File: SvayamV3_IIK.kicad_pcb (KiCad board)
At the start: 6 copper layers, 131.4 x 90 mm, 290 parts, among them J1 USB_C_Receptacle_USB2.0_16P, J10 Micro_SD_Card_Det1, J11 BUZZER, J12 ADC, J13 CAN, J14 SERIAL5, J15 SAFETY, J16 POWER2, J17 I2C, J18 CAN2, J19 Channel 1, J2 GPS, J20 Channel 5, J21 Channel 9, J22 Channel 13, J23 Channel 2, J24 Channel 6, J25 Channel 10, J26 Channel 14, J27 Channel 3, J28 Channel 7, J29 Channel 11, J3 SPI, J30 Channel 15, J31 Channel 4, J32 Channel 8, J33 Channel 12, J34 Channel 16, J4 TELEM1, J5 TELEM2, J6 SBUS, J7 Conn_01x05_Pin, J8 SERIAL4, J9 POWER1, Q1 AO3400A, SW1 SK-3296S-01-L3, SW2 TS-1010A-B, U1 STM32H743IIK6, U10 TPS2120YFPR, U11 TPS63070, U12 RT9080-33GJ5, U13 RT9080-33GJ5, U14 AP22804AW5, U15 USBLC6-2SC6, U16 TPS2553DBVT, U17 TPS2553DBVT, U18 TPS2553DBVT, U19 TPS2553DBVT, U2 FM25CL64B, U20 TPS2553DBVT, U21 TPS2553DBVT, U22 TPS2553DBVT, U23 TPS2553DBVT, U24 TPS2553DBVT, U3 TJA1051TK-3, U4 TJA1051TK-3, U5 BMP388, U6 DPS310XTSA1, U7 BMI088, U8 BMI270, U9 BMM150, Y1 X50328MSB2GI

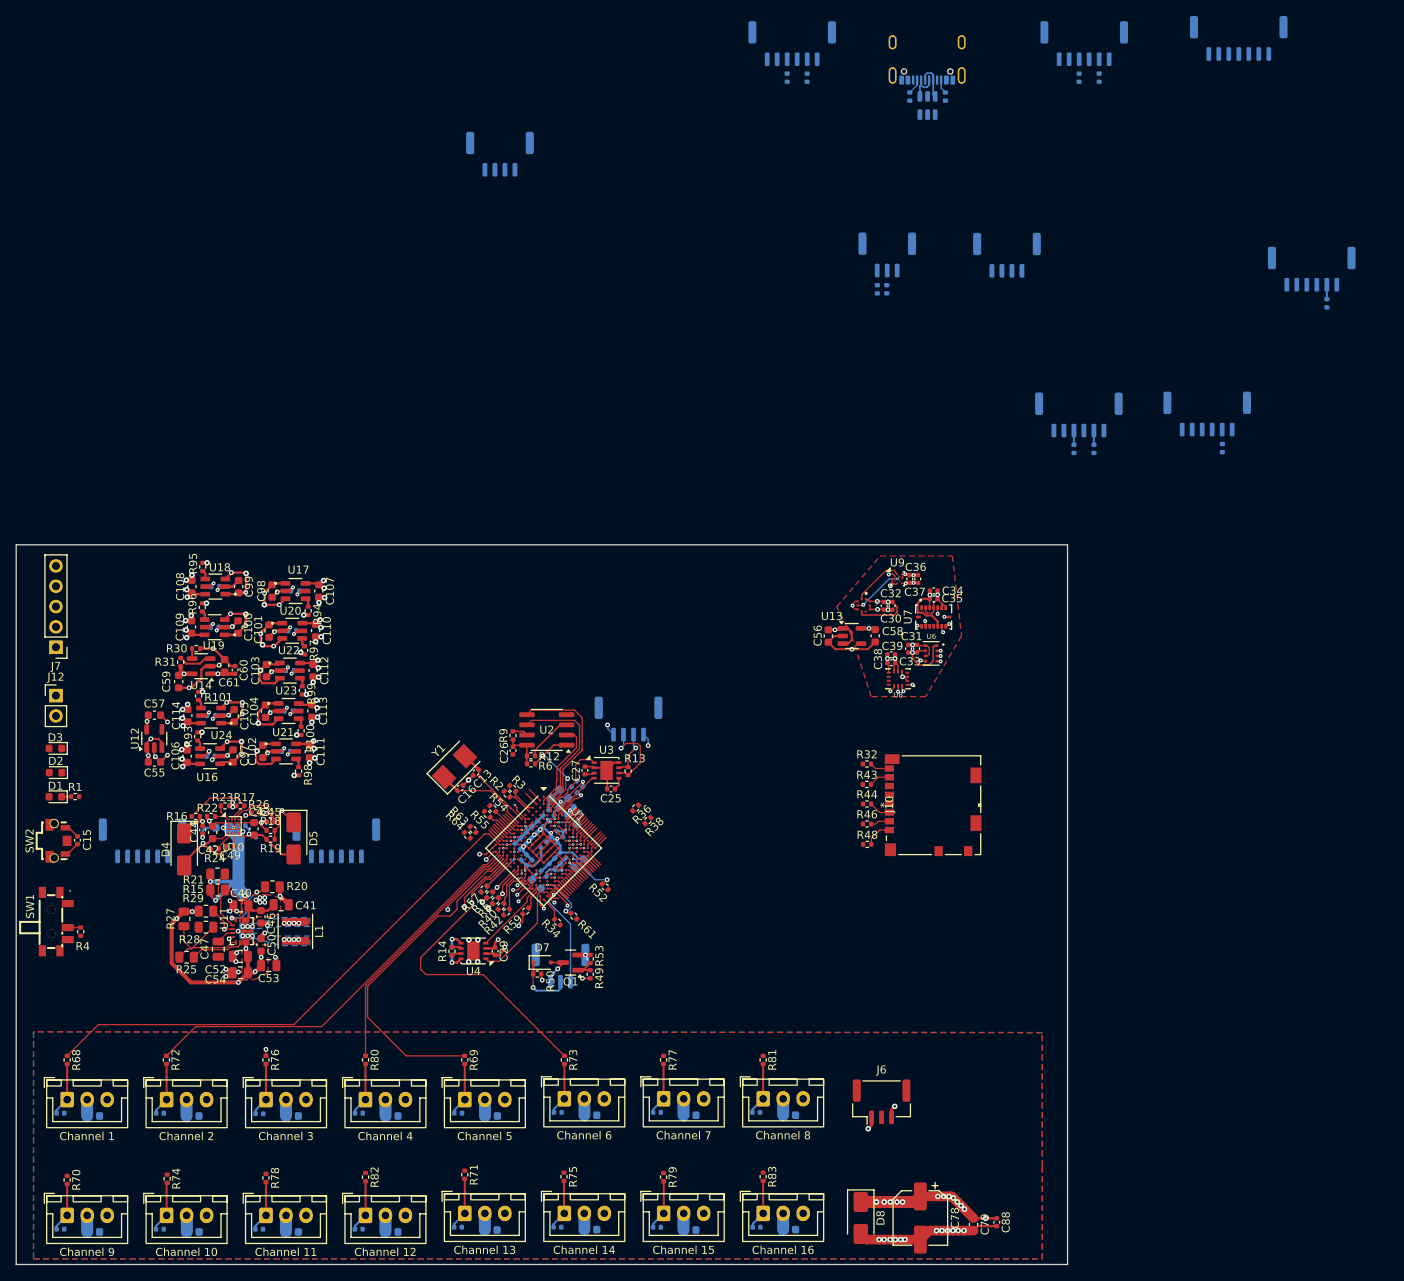
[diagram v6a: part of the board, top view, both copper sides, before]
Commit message: Repo: siap publikasi — README, docs/ (STATUS·DESIGN·STACKUP·schematic·BOM·report), fabrication gate, .gitignore/.gitattributes
- README.md: spesifikasi board, arsitektur, peta konektor, status jujur (not fab-ready)
- docs/: STATUS.md (DRC 765 item + 6 short terdaftar), DESIGN.md (keputusan + referensi),
  STACKUP.md (6-layer 1.5584mm terverifikasi), schematic.pdf, bom.csv, board-stats.txt,
  images/ (preview PCB F+B), reports/ (ERC + DRC mentah, bertanggal)
- fabrication/README.md: release gate + perintah ekspor gerber/drill/pos/step
- .gitignore: whitelist + blokir .history/ output/ *-backups/ *.kicad_prl *.lck
- untrack: .kicad_prl, 23 backup zip, Library/tps63070.pretty/catboy.kicad_mod (0 referensi)

Verifikasi: ERC 0E/17W, parity 0, 290 fp/262 net/1005 node, DRC 765 (6 short, 7 unconnected) — kicad-cli 10.0.6
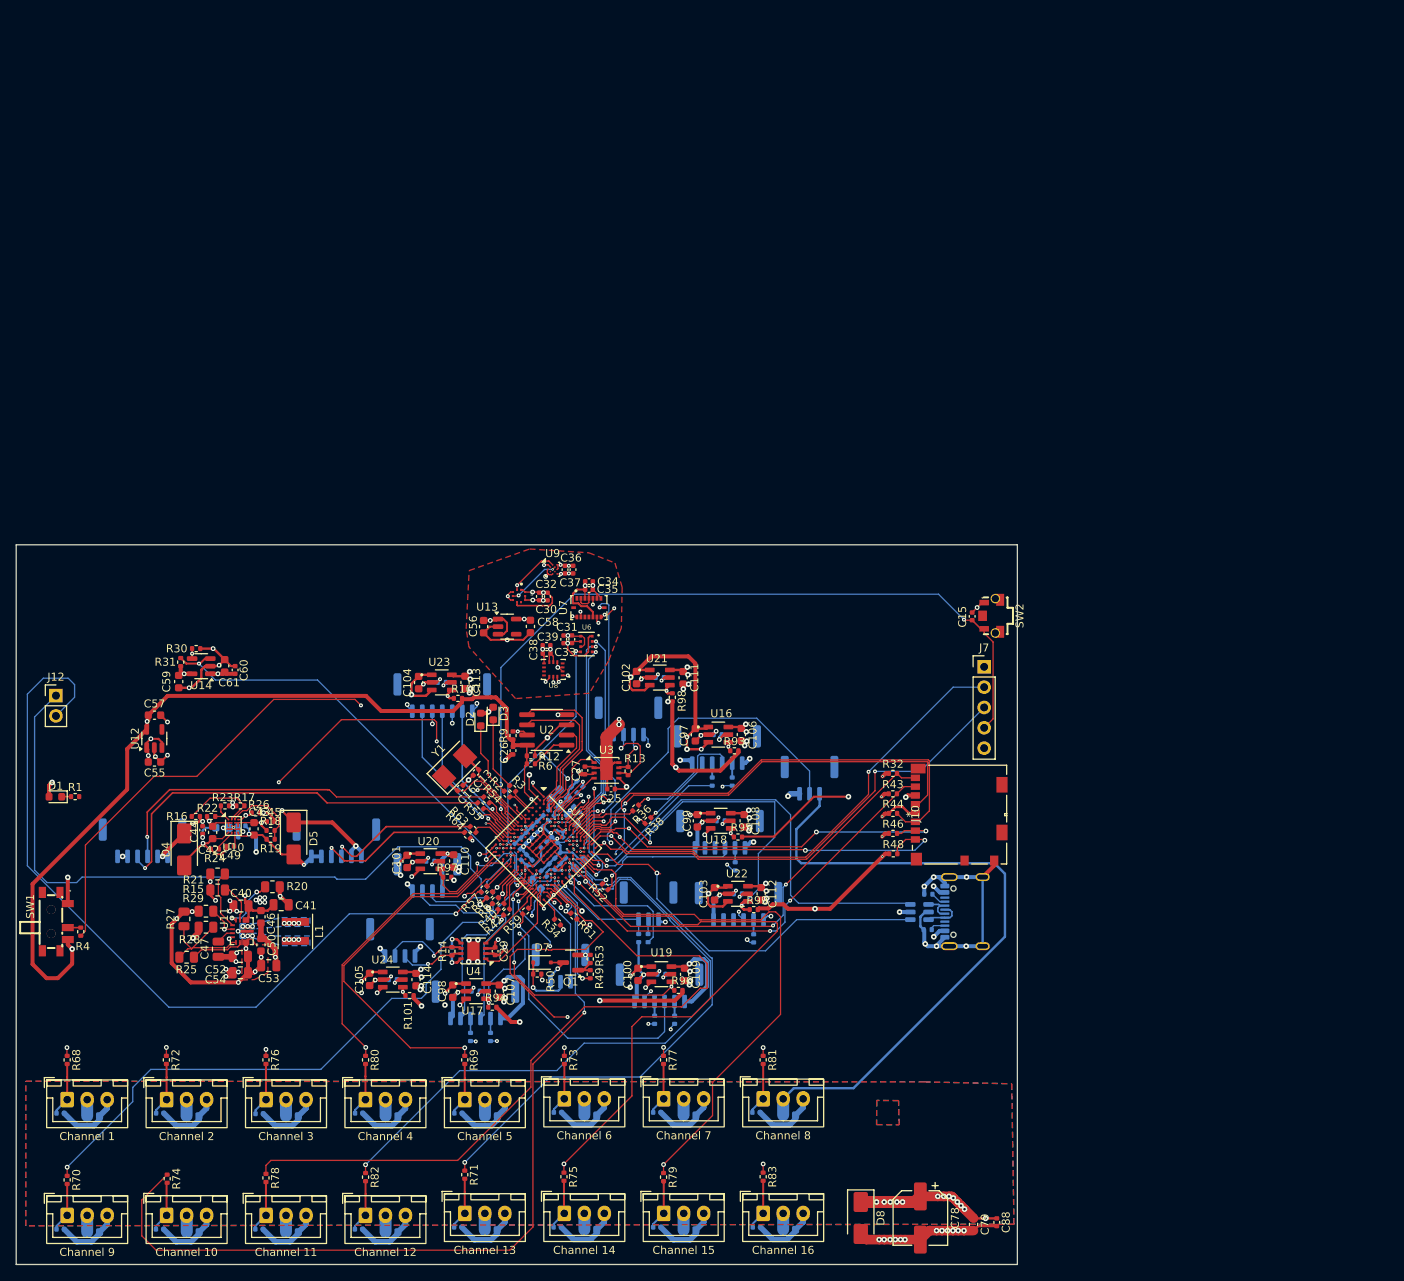
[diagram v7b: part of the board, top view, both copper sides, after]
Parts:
- J6: moved to B.Cu
- moved J3 129.1 mm to (87.0, 113.7)
- moved J5 126.3 mm to (91.2, 152.1)
- moved R39 126.3 mm to (93.1, 156.3), turned to -90 degrees
- moved R41 126.3 mm to (90.6, 156.3)
- moved SW2 120.0 mm to (155.7, 103.7), turned to 0 degrees
- moved J7 116.1 mm to (154.8, 110.1), turned to 0 degrees
- moved C15 115.3 mm to (153.3, 103.7), turned to -90 degrees
- moved R33 106.9 mm to (126.0, 144.0)
- moved J2 106.9 mm to (124.1, 139.7)
- moved J1 106.4 mm to (152.2, 140.7), turned to -90 degrees
- moved J17 106.1 mm to (85.2, 136.1)
- moved R45 104.1 mm to (147.7, 142.9), turned to 180 degrees
- moved U15 100.8 mm to (146.7, 140.7), turned to 180 degrees
- moved R47 99.7 mm to (147.8, 138.5), turned to 180 degrees
- moved J4 99.2 mm to (121.4, 120.1)
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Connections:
- R77 pad 1: TIM4_CH3 -> TIM4_CH2
- R81 pad 1: TIM4_CH2 -> TIM4_CH3
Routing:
- net GND: track 216.0 -> 461.1 mm, vias 107 -> 129
- net +3V3_FMU: track 49.1 -> 285.7 mm, vias 21 -> 29
- net +VBUS: track 0.00 -> 173.9 mm, vias 0 -> 4
- net +5V_PERIPH: track 75.3 -> 239.4 mm, vias 24 -> 25
- net +5V_IN: track 42.0 -> 149.9 mm, vias 10 -> 12
- net TIM5_CH1: track 0.48 -> 108.2 mm, vias 1 -> 2
- net Net-(J12-Pin_2): track 0.00 -> 103.4 mm, vias 0 -> 1
- net NRST: track 3.86 -> 99.8 mm, vias 0 -> 2
- net TIM8_CH1: track 1.92 -> 93.3 mm, vias 0 -> 1
- net Net-(U1-BOOT0): track 0.48 -> 89.7 mm, vias 1 -> 2
- net TIM5_CH2: track 0.48 -> 86.3 mm, vias 1 -> 2
- net Net-(J12-Pin_1): track 0.00 -> 85.6 mm
- net TIM8_CH2: track 1.92 -> 80.8 mm, vias 0 -> 2
- net +VSERVO: track 53.0 -> 131.5 mm, vias 14 -> 13
- net TIM1_CH2: track 1.92 -> 74.7 mm, vias 0 -> 1
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- added copper zone on In3.Cu, net +3V3_FMU
- added copper zone on In1.Cu, net GND
- added copper zone on In4.Cu, net GND
- removed copper zone on F.Cu, net /Power/VIN_BB
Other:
- board size 131.4 x 90 mm -> 125.1 x 90 mm

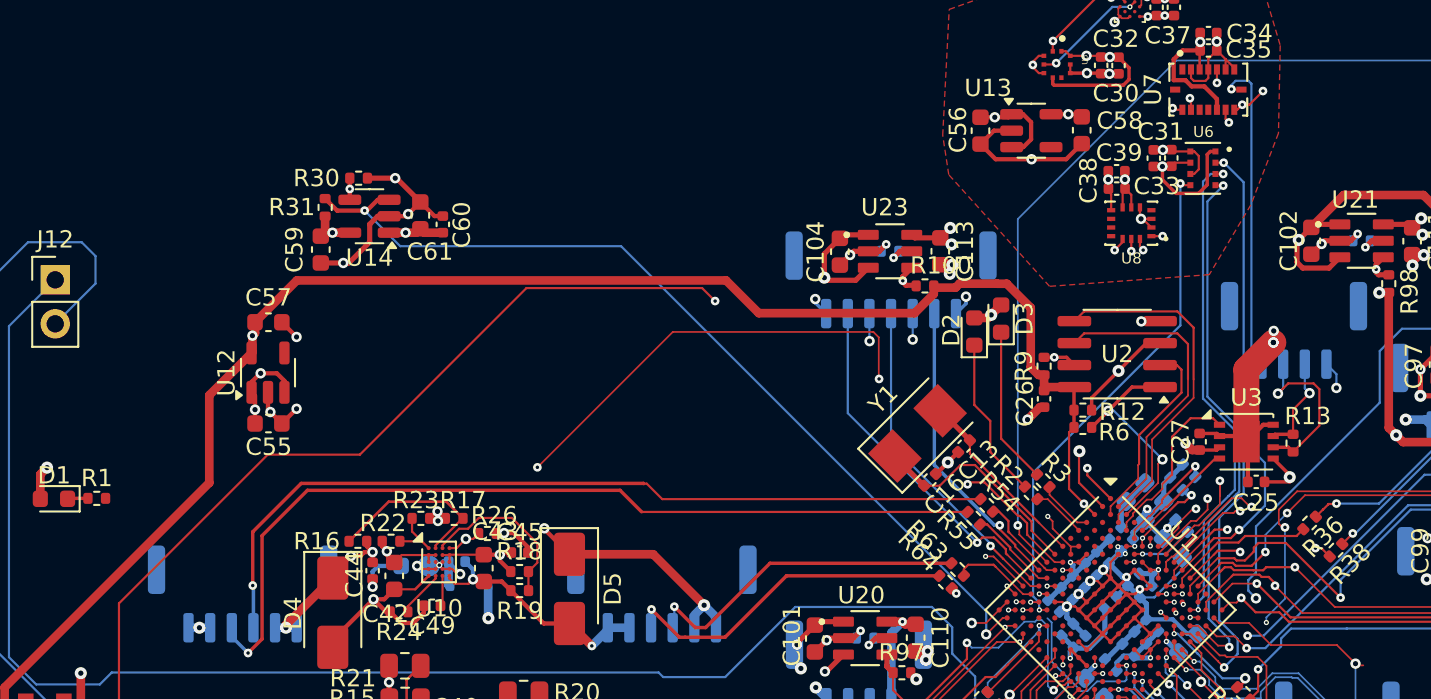
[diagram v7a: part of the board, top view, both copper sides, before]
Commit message: PCB: 7 open connection ditutup — unconnected 7->0, DRC 771->760 (321E/439W)
Ditutup: R1.2<->J9.6 (GND), C24.2<->via (GND), U1.K4 (+3V3_FMU/VDD, pin power MCU),
gap GND stub 0,011mm, +VBRICK1, +VBRICK2, SPI1_MISO antara U7.10<->U7.15.
Efek samping: via_dangling 46->43, track_dangling 11->10.

Masih terbuka: 5 short di pad MP JST-GH (J17 x2, J11) — langkah berikutnya.

Verifikasi: kicad-cli 10.0.6 pcb drc --severity-all --schematic-parity
  unconnected 0, parity 0, 321 error / 439 warning, board 125,145x89,96 mm, 475 via.
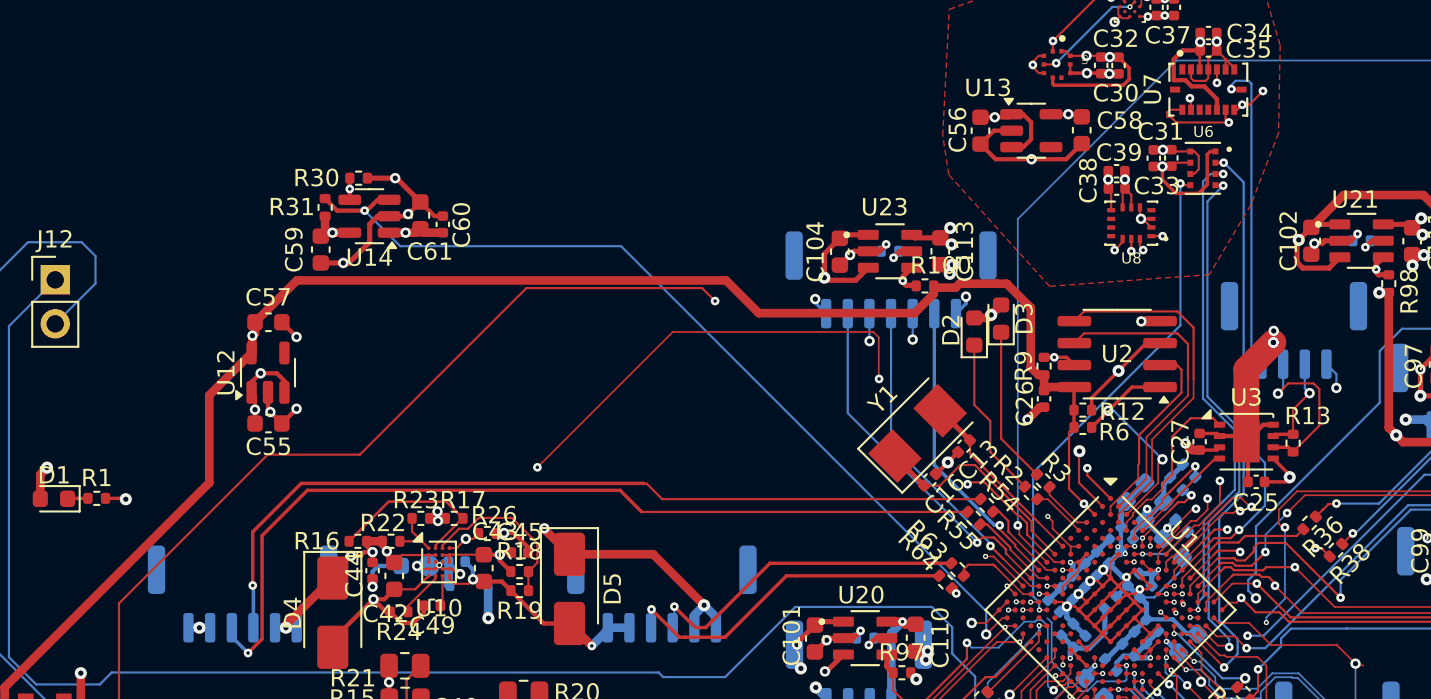
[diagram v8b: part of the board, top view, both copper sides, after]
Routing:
- net SPI1_MISO: track 29.2 -> 33.4 mm, vias 3 -> 2
- net +VBRICK2: track 20.1 -> 23.3 mm
- net GND: track 461.1 -> 463.9 mm, vias 129 -> 130
- net +3V3_FMU: track 285.7 -> 287.9 mm
- net +VBRICK1: track 14.1 -> 15.0 mm
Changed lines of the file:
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@@
 	)
 	(segment
-		(start 112.09625 111.39375)
-		(end 112.97125 111.39375)
-		(width 0.3)
-		(layer "F.Cu")
-		(net "GND")
-	)
-	(segment
 		(start 84.6725 112.2125)
 		(end 84.885 112)
@@
 	)
 	(segment
+		(start 111.5 111.99)
+		(end 111.5 111.55)
+		(width 0.3)
+		(layer "F.Cu")
+		(net "GND")
+	)
+	(segment
 		(start 97.8827 134.559657)
 		(end 98.34232 135.019276)
@@
 	)
 	(segment
-		(start 111.91625 111.57375)
-		(end 112.09625 111.39375)
-		(width 0.3)
-		(layer "F.Cu")
-		(net "GND")
-	)
-	(segment
 		(start 64.375 143.55)
 		(end 64.85 144.025)
@@
 	)
 	(segment
+		(start 111.94 111.55)
+		(end 112.09625 111.39375)
+		(width 0.3)
+		(layer "F.Cu")
+		(net "GND")
+	)
+	(segment
 		(start 100.55 108.36625)
 		(end 100.56 108.37625)
@@
 	)
 	(segment
+		(start 42.775 126.275)
+		(end 42.825 126.325)
+		(width 0.2)
+		(layer "F.Cu")
+		(net "GND")
+	)
+	(segment
 		(start 101.5025 97.405)
 		(end 101.5025 97.771)
@@
 	)
 	(segment
-		(start 111.32125 112.16875)
-		(end 111.91625 111.57375)
-		(width 0.3)
-		(layer "F.Cu")
-		(net "GND")
-	)
-	(segment
 		(start 79.6 149.15)
 		(end 80.235 149.15)
@@
 	)
 	(segment
+		(start 112.09625 111.39375)
+		(end 112.97125 111.39375)
+		(width 0.3)
+		(layer "F.Cu")
+		(net "GND")
+	)
+	(segment
 		(start 119.375 118.625)
 		(end 119.475 118.525)
@@
 	)
 	(segment
-		(start 102.442321 131.342321)
-		(end 102.45 131.35)
-		(width 0.1)
-		(layer "F.Cu")
-		(net "GND")
-	)
-	(segment
 		(start 146.1768 126.12975)
 		(end 145.19525 126.12975)
@@
 	)
 	(segment
+		(start 41.6575 126.275)
+		(end 42.775 126.275)
+		(width 0.2)
+		(layer "F.Cu")
+		(net "GND")
+	)
+	(segment
 		(start 83.4375 134.35)
 		(end 84.29 134.35)
@@
 	)
 	(segment
+		(start 111.32125 112.16875)
+		(end 111.5 111.99)
+		(width 0.3)
+		(layer "F.Cu")
+		(net "GND")
+	)
+	(segment
 		(start 66.06 129.095001)
 		(end 65.244999 128.28)
@@
 	)
 	(segment
+		(start 111.5 111.55)
+		(end 111.94 111.55)
+		(width 0.3)
+		(layer "F.Cu")
+		(net "GND")
+	)
+	(segment
 		(start 56.9175 111.47)
 		(end 56.9175 110.437501)
@@
 	)
 	(via
-		(at 111.91625 111.57375)
+		(at 111.5 111.55)
 		(size 0.6)
 		(drill 0.3)
@@
 	)
 	(via
+		(at 42.825 126.325)
+		(size 0.7)
+		(drill 0.3)
+		(layers "F.Cu" "B.Cu")
+		(net "GND")
+	)
+	(via
 		(at 62.885 130.955)
 		(size 0.6)
@@
 	)
 	(segment
+		(start 100.325 127.959712)
+		(end 100.342356 127.942356)
+		(width 0.25)
+		(layer "B.Cu")
+		(net "GND")
+	)
+	(segment
 		(start 106.35 166.575)
 		(end 106.35 166.1)
@@
 	)
 	(segment
+		(start 100.325 129.325)
+		(end 100.325 127.959712)
+		(width 0.25)
+		(layer "B.Cu")
+		(net "GND")
+	)
+	(segment
 		(start 77.1 165.85)
 		(end 78.677 167.427)
@@
 	)
 	(segment
+		(start 97.8827 130.4423)
+		(end 97.8827 129.963463)
+		(width 0.1)
+		(layer "F.Cu")
+		(net "+3V3_FMU")
+	)
+	(segment
 		(start 142.8733 128.37475)
 		(end 143.67305 127.575)
@@
 	)
 	(segment
+		(start 96.963462 131.361538)
+		(end 97.8827 130.4423)
+		(width 0.1)
+		(layer "F.Cu")
+		(net "+3V3_FMU")
+	)
+	(segment
 		(start 97.611178 121.176178)
 		(end 97.611178 119.866178)
@@
 	)
 	(segment
+		(start 96.963462 131.80194)
+		(end 96.963462 131.361538)
+		(width 0.1)
+		(layer "F.Cu")
+		(net "+3V3_FMU")
+	)
+	(segment
 		(start 40.2275 144.15)
 		(end 40.2275 144.7775)
@@
 	)
 	(segment
+		(start 56.745 128.755)
+		(end 57.64 128.755)
+		(width 0.5)
+		(layer "F.Cu")
+		(net "+VBRICK1")
+	)
+	(segment
 		(start 60.325 129.55)
 		(end 60.725 129.55)
@@
 		(start 67.01 128.055)
 		(end 68.46 129.505)
-		(width 0.25)
+		(width 0.5)
 		(layer "F.Cu")
 		(net "+VBRICK2")
@@
 	)
 	(segment
+		(start 64.435 129.53)
+		(end 65.485 129.53)
+		(width 0.7)
+		(layer "In3.Cu")
+		(net "+VBRICK2")
+	)
+	(segment
+		(start 65.485 129.53)
+		(end 67.01 128.005)
+		(width 0.7)
+		(layer "In3.Cu")
+		(net "+VBRICK2")
+	)
+	(segment
 		(start 59.12 132.510001)
 		(end 60.725 130.905001)
@@
 	)
 	(segment
+		(start 103 103.971998)
+		(end 103 104.225)
+		(width 0.127)
+		(layer "F.Cu")
+		(net "SPI1_MISO")
+	)
+	(segment
 		(start 106.83 127.12)
 		(end 106.94 127.01)
@@
 	)
 	(segment
+		(start 103.87 103.823499)
+		(end 103.148499 103.823499)
+		(width 0.127)
+		(layer "F.Cu")
+		(net "SPI1_MISO")
+	)
+	(segment
 		(start 103.396178 129.946178)
 		(end 104.750659 128.591697)
@@
 	)
 	(segment
-		(start 103.399999 103.823499)
-		(end 103.3075 103.731)
+		(start 103 104.225)
+		(end 103.194 104.225)
+		(width 0.127)
+		(layer "F.Cu")
+		(net "SPI1_MISO")
+	)
+	(segment
+		(start 103.525 104.556)
+		(end 106.5575 104.556)
+		(width 0.127)
+		(layer "F.Cu")
+		(net "SPI1_MISO")
+	)
+	(segment
+		(start 103.148499 103.823499)
+		(end 103 103.971998)
 		(width 0.127)
 		(layer "F.Cu")
@@
 	)
 	(segment
-		(start 103.87 103.823499)
-		(end 103.399999 103.823499)
+		(start 103.194 104.225)
+		(end 103.525 104.556)
 		(width 0.127)
 		(layer "F.Cu")
@@
 		(size 0.5)
 		(drill 0.2)
-		(layers "F.Cu" "B.Cu")
-		(net "SPI1_MISO")
-	)
-	(via
-		(at 103.3075 103.731)
-		(size 0.5)
-		(drill 0.2)
